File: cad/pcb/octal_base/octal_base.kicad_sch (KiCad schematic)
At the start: 8 parts, among them J1 U6A Base, J2 Pin header

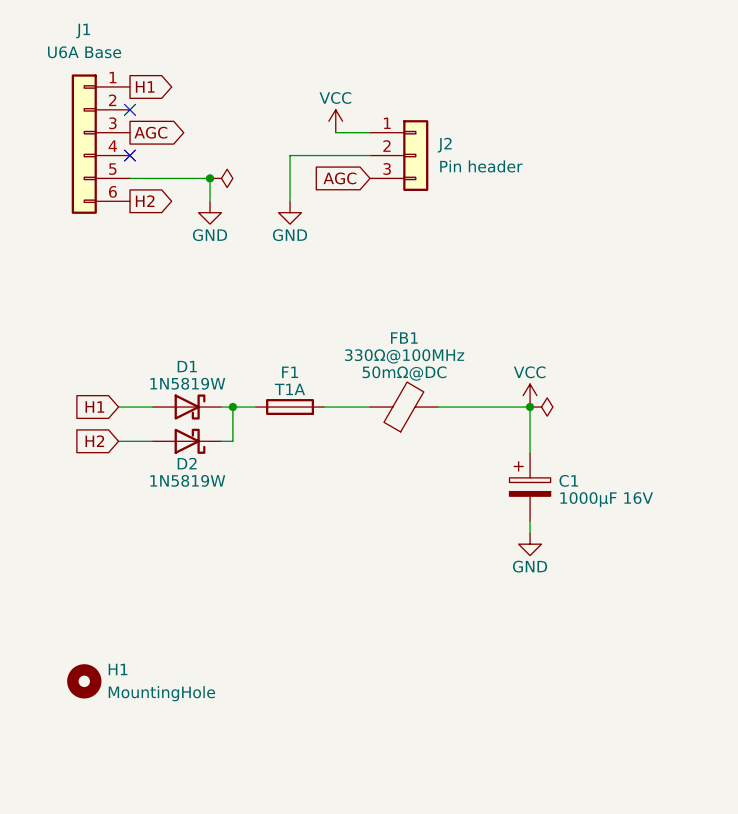
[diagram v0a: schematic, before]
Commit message: Change: Use octal socket, Add: Anode voltage detection
change pin socket to 5way
- more stability
- extra pin
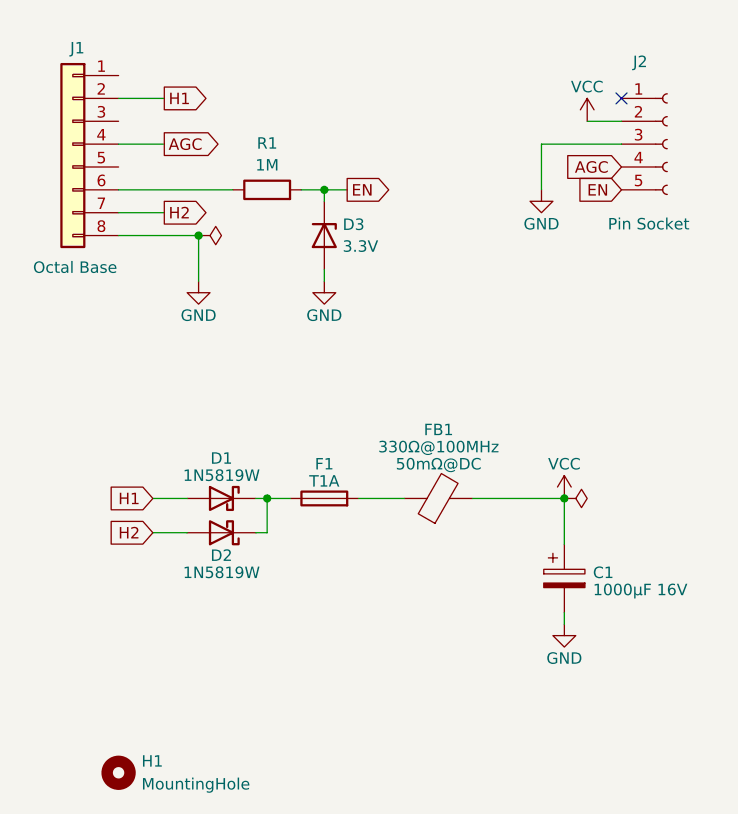
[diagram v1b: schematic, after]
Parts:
- removed J1: U6A Base, Retronics_Connectors:U6A_Base, symbol Connector_Generic:Conn_01x06
- removed J2: Pin header, Retronics_Connectors:PinSocket_1x03_P2.54mm_Vertical, symbol Connector_Generic:Conn_01x03
- added D3: 3.3V, Diode_SMD:D_0603_1608Metric_Pad1.05x0.95mm_HandSolder, symbol Device:D_Zener
- added J1: Octal Base, Valve:Valve_Octal, symbol Connector_Generic:Conn_01x08
- added J2: Pin Socket, PinSocket_1x05_P2.54mm_Vertical, symbol Connector:Conn_01x05_Socket
- added R1: 1M, Resistor_SMD:R_1206_3216Metric_Pad1.30x1.75mm_HandSolder, symbol Device:R
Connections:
- net AGC: now also J1.4 (Pin_4), J2.4 (Pin_4)
- net GND: now also D3.2 (A), J1.8 (Pin_8), J2.3 (Pin_3)
- net H1: now also J1.2 (Pin_2)
- net H2: now also J1.7 (Pin_7)
- net VCC: now also J2.2 (Pin_2)
- new net: J1.6 (Pin_6), R1.1
- new net EN: D3.1 (K), J2.5 (Pin_5), R1.2
- no-connect marks 2 -> 1
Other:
- company: (none) -> Martin Wagner DL2WAG
- title: (none) -> Adaptor octal socket
- moved on the sheet: C1, D1, D2, F1, FB1, H1

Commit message: Change: Pcb to octal
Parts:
- C1: footprint Retronics_Passives:CP_Radial_D8.0mm_P3.50mm_H21mm -> CP_Radial_D8.0mm_P3.50mm_H21mm
- D1, D2: footprint Retronics_Discrete:D_SOD-323_HandSoldering -> D_SOD-323_HandSoldering
- F1: footprint Retronics_Passives:Fuse_1206_3216Metric -> Fuse_1206_3216Metric
- FB1: footprint Retronics_Passives:L_0805_2012Metric_Pad1.15x1.40mm_HandSolder -> L_0805_2012Metric_Pad1.15x1.40mm_HandSolder
- J1: footprint Valve:Valve_Octal -> Library:Valve_Octal_Base
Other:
- title: Adaptor octal socket -> Adaptor octal base
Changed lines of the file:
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@@
 	(paper "A4")
 	(title_block
-		(title "Adaptor octal socket")
+		(title "Adaptor octal base")
 		(date "2025-01-06")
-		(rev "2-A")
+		(rev "1-A")
 		(company "Martin Wagner DL2WAG")
 		(comment 1 "Based on Retronics 6U5")
@@
 			)
 		)
-		(property "Footprint" "Retronics_Passives:Fuse_1206_3216Metric"
+		(property "Footprint" "Fuse_1206_3216Metric"
 			(at 62.23 84.328 90)
 			(effects
@@
 			)
 		)
-		(property "Footprint" "Retronics_Passives:CP_Radial_D8.0mm_P3.50mm_H21mm"
+		(property "Footprint" "CP_Radial_D8.0mm_P3.50mm_H21mm"
 			(at 89.8652 95.25 0)
 			(effects
@@
 			)
 		)
-		(property "Footprint" "Retronics_Discrete:D_SOD-323_HandSoldering"
+		(property "Footprint" "D_SOD-323_HandSoldering"
 			(at 50.8 81.915 0)
 			(effects
@@
 			)
 		)
-		(property "Footprint" "Retronics_Passives:L_0805_2012Metric_Pad1.15x1.40mm_HandSolder"
+		(property "Footprint" "L_0805_2012Metric_Pad1.15x1.40mm_HandSolder"
 			(at 74.93 84.328 90)
 			(effects
@@
 			)
 		)
-		(property "Footprint" "Retronics_Discrete:D_SOD-323_HandSoldering"
+		(property "Footprint" "D_SOD-323_HandSoldering"
 			(at 50.8 86.995 0)
 			(effects
@@
 			)
 		)
-		(property "Footprint" "Valve:Valve_Octal"
+		(property "Footprint" "Library:Valve_Octal_Base"
 			(at 34.29 43.18 0)
 			(effects
